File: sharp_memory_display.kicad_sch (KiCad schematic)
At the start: 14 parts, among them J1 Conn_01x05, J2 Conn_01x10, J3 Conn_01x05_Male

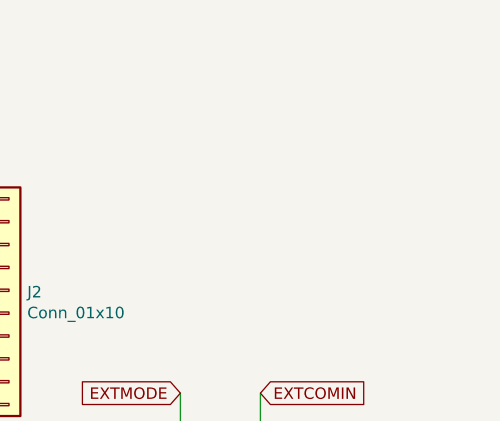
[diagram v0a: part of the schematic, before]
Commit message: add solderable pad
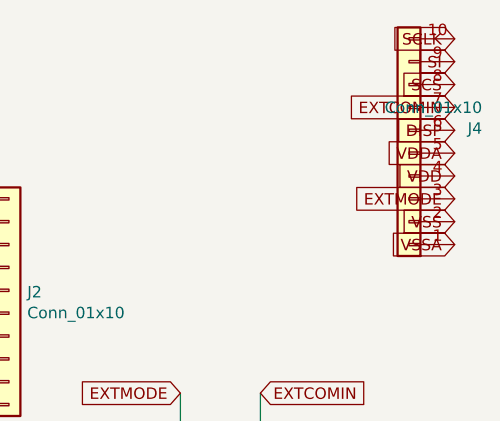
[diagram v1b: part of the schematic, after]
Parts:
- added J4: Conn_01x10, Connector_FFC-FPC:Hirose_FH12-10S-0.5SH_1x10-1MP_P0.50mm_Horizontal, symbol Connector_Generic:Conn_01x10
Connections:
- net DISP: now also J4.6 (Pin_6)
- net EXTCOMIN: now also J4.7 (Pin_7)
- net EXTMODE: now also J4.3 (Pin_3)
- net GND: now also J4.2 (Pin_2)
- net GNDA: now also J4.1 (Pin_1)
- net SCLK: now also J4.10 (Pin_10)
- net SCS: now also J4.8 (Pin_8)
- net SI: now also J4.9 (Pin_9)
- net VDD: now also J4.4 (Pin_4)
- net VDDA: now also J4.5 (Pin_5)
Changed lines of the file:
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@@
+    )
+  )
+  (global_label "SCLK" (shape input) (at 247.65 53.34 180) (fields_autoplaced)
+    (effects (font (size 1.27 1.27)) (justify right))
+    (property "Intersheet References" "${INTERSHEET_REFS}" (id 0) (at 54.61 -17.78 0)
+      (effects (font (size 1.27 1.27)) hide)
+    )
+  )
+  (global_label "SI" (shape input) (at 247.65 55.88 180) (fields_autoplaced)
+    (effects (font (size 1.27 1.27)) (justify right))
+    (property "Intersheet References" "${INTERSHEET_REFS}" (id 0) (at 54.61 -17.78 0)
+      (effects (font (size 1.27 1.27)) hide)
+    )
+  )
+  (global_label "SCS" (shape input) (at 247.65 58.42 180) (fields_autoplaced)
+    (effects (font (size 1.27 1.27)) (justify right))
+    (property "Intersheet References" "${INTERSHEET_REFS}" (id 0) (at 54.61 -17.78 0)
+      (effects (font (size 1.27 1.27)) hide)
+    )
+  )
+  (global_label "EXTCOMIN" (shape input) (at 247.65 60.96 180) (fields_autoplaced)
+    (effects (font (size 1.27 1.27)) (justify right))
+    (property "Intersheet References" "${INTERSHEET_REFS}" (id 0) (at 54.61 -17.78 0)
+      (effects (font (size 1.27 1.27)) hide)
+    )
+  )
+  (global_label "DISP" (shape input) (at 247.65 63.5 180) (fields_autoplaced)
+    (effects (font (size 1.27 1.27)) (justify right))
+    (property "Intersheet References" "${INTERSHEET_REFS}" (id 0) (at 54.61 -17.78 0)
+      (effects (font (size 1.27 1.27)) hide)
+    )
+  )
+  (global_label "VDDA" (shape input) (at 247.65 66.04 180) (fields_autoplaced)
+    (effects (font (size 1.27 1.27)) (justify right))
+    (property "Intersheet References" "${INTERSHEET_REFS}" (id 0) (at 54.61 -17.78 0)
+      (effects (font (size 1.27 1.27)) hide)
+    )
+  )
+  (global_label "VDD" (shape input) (at 247.65 68.58 180) (fields_autoplaced)
+    (effects (font (size 1.27 1.27)) (justify right))
+    (property "Intersheet References" "${INTERSHEET_REFS}" (id 0) (at 54.61 -17.78 0)
+      (effects (font (size 1.27 1.27)) hide)
+    )
+  )
+  (global_label "EXTMODE" (shape input) (at 247.65 71.12 180) (fields_autoplaced)
+    (effects (font (size 1.27 1.27)) (justify right))
+    (property "Intersheet References" "${INTERSHEET_REFS}" (id 0) (at 54.61 -17.78 0)
+      (effects (font (size 1.27 1.27)) hide)
+    )
+  )
+  (global_label "VSS" (shape input) (at 247.65 73.66 180) (fields_autoplaced)
+    (effects (font (size 1.27 1.27)) (justify right))
+    (property "Intersheet References" "${INTERSHEET_REFS}" (id 0) (at 54.61 -17.78 0)
+      (effects (font (size 1.27 1.27)) hide)
+    )
+  )
+  (global_label "VSSA" (shape input) (at 247.65 76.2 180) (fields_autoplaced)
+    (effects (font (size 1.27 1.27)) (justify right))
+    (property "Intersheet References" "${INTERSHEET_REFS}" (id 0) (at 54.61 -17.78 0)
+      (effects (font (size 1.27 1.27)) hide)
     )
   )
@@
     (pin "9")
   )
+  (symbol (lib_id "Connector_Generic:Conn_01x10") (at 242.57 66.04 180) (unit 1)
+    (in_bom yes) (on_board yes)
+    (property "Reference" "J4" (id 0) (at 250.698 63.2968 0)
+      (effects (font (size 1.27 1.27)) (justify left))
+    )
+    (property "Value" "Conn_01x10" (id 1) (at 250.698 60.9854 0)
+      (effects (font (size 1.27 1.27)) (justify left))
+    )
+    (property "Footprint" "Connector_FFC-FPC:Hirose_FH12-10S-0.5SH_1x10-1MP_P0.50mm_Horizontal" (id 2) (at 242.57 66.04 0)
+      (effects (font (size 1.27 1.27)) hide)
+    )
+    (property "Datasheet" "~" (id 3) (at 242.57 66.04 0)
+      (effects (font (size 1.27 1.27)) hide)
+    )
+    (property "LCSC" "C376059" (id 4) (at 242.57 66.04 0)
+      (effects (font (size 1.27 1.27)) hide)
+    )
+    (pin "1")
+    (pin "10")
+    (pin "2")
+    (pin "3")
+    (pin "4")
+    (pin "5")
+    (pin "6")
+    (pin "7")
+    (pin "8")
+    (pin "9")
+  )
   (sheet_instances
     (path "/" (page "1"))
@@
       (reference "J3") (unit 1) (value "Conn_01x05_Male") (footprint "Connector_JST:JST_SH_SM05B-SRSS-TB_1x05-1MP_P1.00mm_Horizontal")
     )
+    (path "/ffcd554b-7538-4995-b7eb-e9238dfe2323"
+      (reference "J4") (unit 1) (value "Conn_01x10") (footprint "Connector_FFC-FPC:Hirose_FH12-10S-0.5SH_1x10-1MP_P0.50mm_Horizontal")
+    )
     (path "/00000000-0000-0000-0000-0000611a96b1"

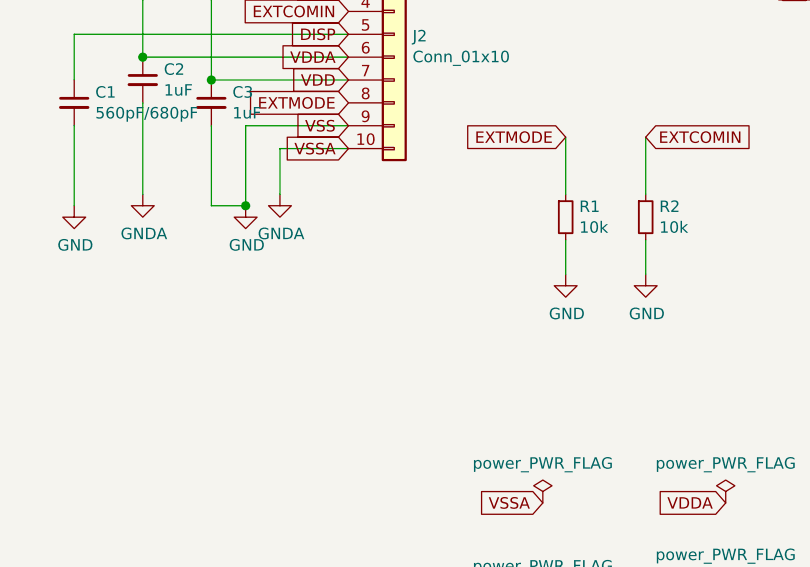
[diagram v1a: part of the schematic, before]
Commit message: add pullup resistor for DISP
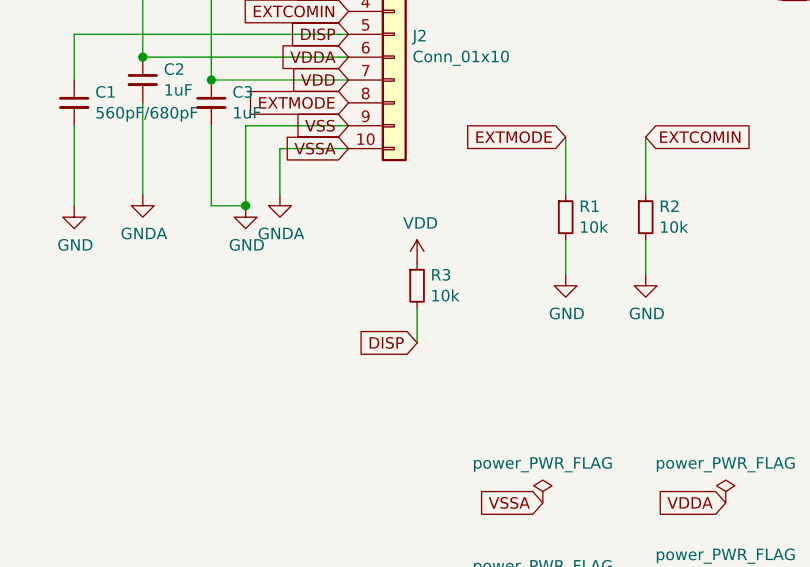
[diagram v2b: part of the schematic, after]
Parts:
- added R3: 10k, Resistor_SMD:R_0603_1608Metric_Pad0.98x0.95mm_HandSolder, symbol Device:R_Small
- FB1, FB2: LCSC 0805 -> C1017
- J2, J4: LCSC C376059 -> C506791
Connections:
- net DISP: now also R3.2
- net VDD: now also R3.1

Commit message: tidy up schematic
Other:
- note added: "17 August 2022"
- note added: "2"
- note added: "LS011B7DH03 Sharp memory display breakout"
- moved on the sheet: C1, C2, C3, FB1, FB2, H1, H2, H3, H4, J3, J4, R1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

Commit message: nice!view compatible
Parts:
- removed J4: Conn_01x10, Connector_FFC-FPC:Hirose_FH12-10S-0.5SH_1x10-1MP_P0.50mm_Horizontal, symbol Connector_Generic:Conn_01x10
- removed R1, R2, R3: 10k, Resistor_SMD:R_0603_1608Metric_Pad0.98x0.95mm_HandSolder, symbol Device:R_Small
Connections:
- net DISP is gone; now on net VDD: C1.1, J2.5 (Pin_5)
- net EXTCOMIN is gone; now on net GND: J2.4 (Pin_4)
- net EXTMODE is gone; now on net GND: J2.8 (Pin_8)
- net GND: now also J1.2 (Pin_2), J3.2 (Pin_2); no longer J1.1 (Pin_1), J3.1 (Pin_1)
- net SCLK: now also J1.4 (Pin_4), J3.4 (Pin_4); no longer J1.5 (Pin_5), J3.5 (Pin_5)
- net SCS: now also J1.1 (Pin_1), J3.1 (Pin_1); no longer J1.3 (Pin_3), J3.3 (Pin_3)
- net SI: now also J1.5 (Pin_5), J3.5 (Pin_5); no longer J1.4 (Pin_4), J3.4 (Pin_4)
- net VDD: now also J1.3 (Pin_3), J3.3 (Pin_3); no longer J1.2 (Pin_2), J3.2 (Pin_2)
